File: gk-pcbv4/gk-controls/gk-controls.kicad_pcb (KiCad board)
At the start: 2 copper layers, 120.6 x 72.2 mm, 95 parts, among them J1 Conn_01x20, J2 Conn_01x03, J3 Conn_01x01, J4 Conn_01x01, J5 Conn_01x01, J6 Conn_01x01, U1 PCAL6416APW, U2 ULN2003A

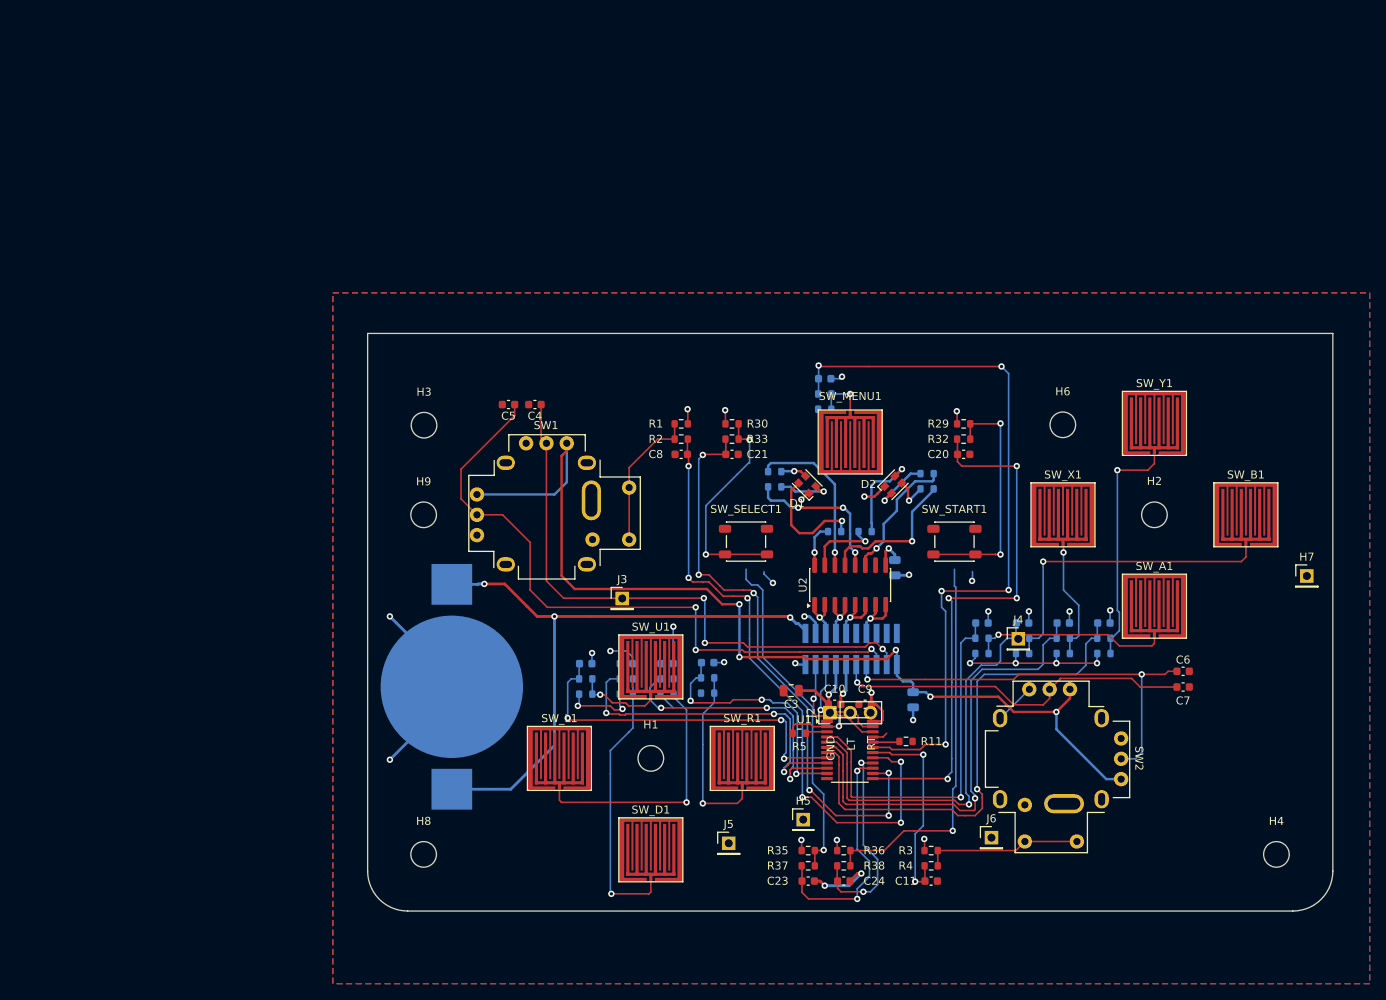
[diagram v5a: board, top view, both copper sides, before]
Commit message: add v3 control board and trigger daughterboard
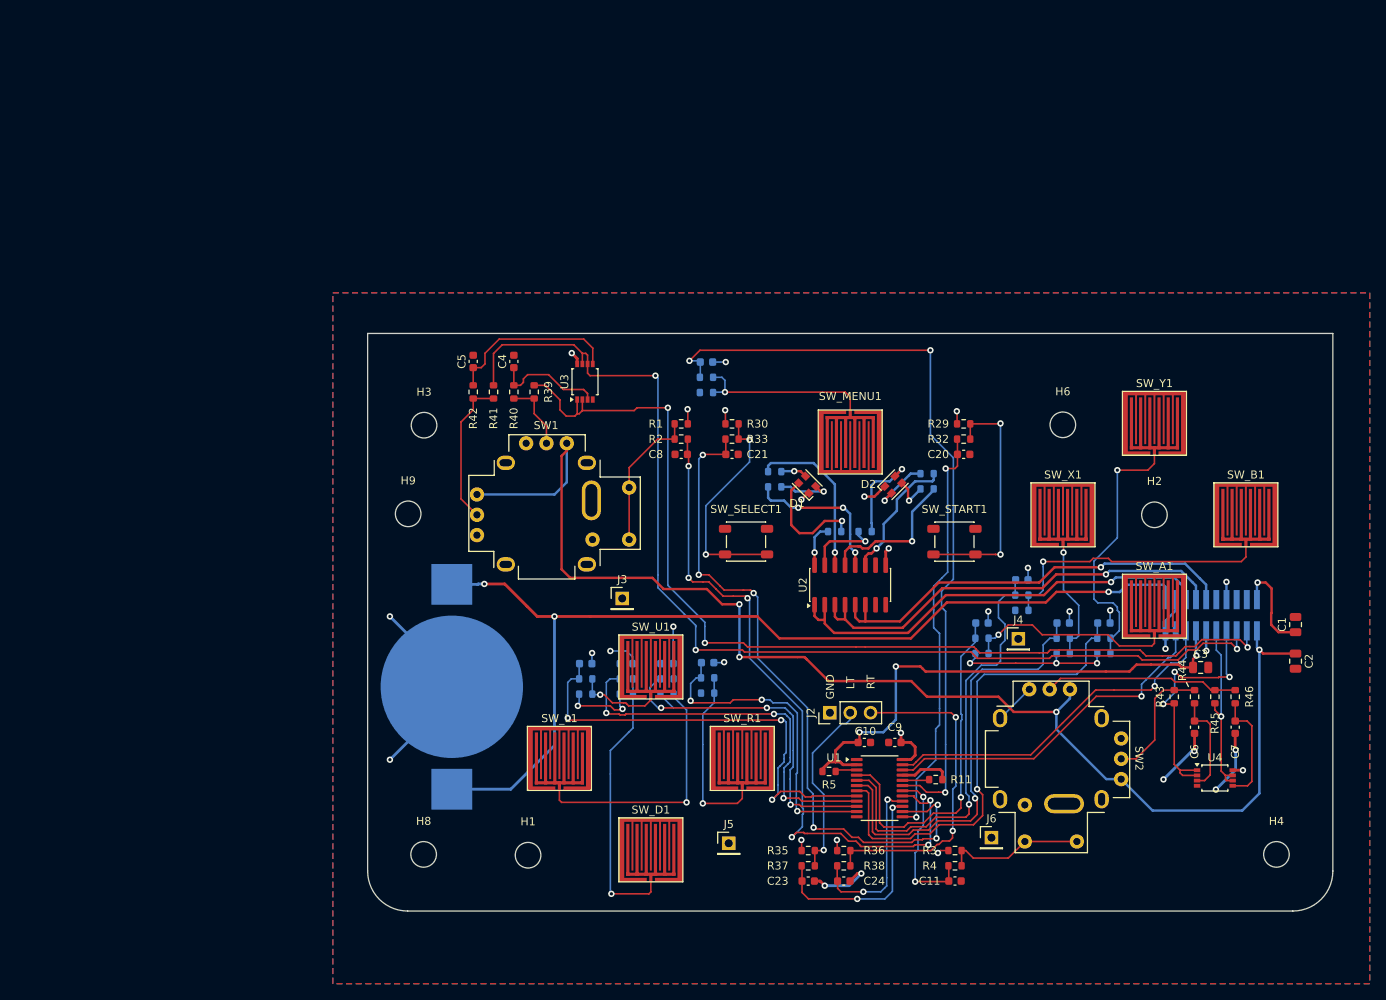
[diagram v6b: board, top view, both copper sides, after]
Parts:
- removed H5, H7: Conn_01x01, Connector_PinHeader_2.54mm:PinHeader_1x01_P2.54mm_Vertical
- added R39: NC, Resistor_SMD:R_0603_1608Metric, F.Cu at (110.5, 67.3)
- added R40: 20k, Resistor_SMD:R_0603_1608Metric, F.Cu at (108.0, 67.3)
- added R41: NC, Resistor_SMD:R_0603_1608Metric, F.Cu at (105.4, 67.3)
- added R42: 20k, Resistor_SMD:R_0603_1608Metric, F.Cu at (102.9, 67.3)
- added R43: NC, Resistor_SMD:R_0603_1608Metric, F.Cu at (190.5, 105.4)
- added R44: 20k, Resistor_SMD:R_0603_1608Metric, F.Cu at (193.0, 105.4)
- added R45: NC, Resistor_SMD:R_0603_1608Metric, F.Cu at (195.6, 105.4)
- added R46: 20k, Resistor_SMD:R_0603_1608Metric, F.Cu at (198.1, 105.4)
- added U3: LMV358DMR2G, Package_SO:OnSemi_Micro8, F.Cu at (116.8, 66.0)
- added U4: LMV358DMR2G, Package_SO:OnSemi_Micro8, F.Cu at (195.6, 115.6)
- C1, C2: moved to F.Cu
- C4, C5, C6, C7: value 10n -> 100n
- moved C3 51.3 mm to (193.8, 101.8), turned to 0 degrees
- moved C1 50.6 mm to (205.7, 96.4), turned to 90 degrees
- moved C2 48.0 mm to (205.7, 101.0)
- moved J1 45.2 mm to (195.1, 95.2)
- moved H1 19.5 mm to (109.7, 125.2)
- moved C22 14.9 mm to (132.0, 63.6)
- moved R31 14.9 mm to (132.0, 67.4)
- moved R34 14.9 mm to (132.0, 65.5)
- moved C7 8.22 mm to (198.1, 109.2), turned to -90 degrees
- moved C6 7.13 mm to (193.0, 109.2), turned to -90 degrees
- moved C5 6.97 mm to (102.9, 63.5), turned to 90 degrees
- moved R11 6.05 mm to (160.7, 115.8)
- moved R5 6.05 mm to (147.4, 114.8)
- moved U1 6.05 mm to (153.7, 116.8)
- moved C10 6.05 mm to (151.8, 111.1)
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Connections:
- C4 pad 1: JOY_A_X -> Net-(U3A-+)
- C5 pad 1: JOY_A_Y -> Net-(U3B-+)
- C6 pad 1: JOY_B_X -> Net-(U4A-+)
- C7 pad 1: JOY_B_Y -> Net-(U4B-+)
- J1 pad 3: JOY_A_X -> JOY_A_X_MCU
- J1 pad 5: JOY_A_Y -> JOY_A_Y_MCU
- J1 pad 7: JOY_B_X -> JOY_B_X_MCU
- J1 pad 9: JOY_B_Y -> JOY_B_Y_MCU
- J3 pad 1: unconnected-(J3-Pin_1-Pad1) -> GND
- J4 pad 1: unconnected-(J4-Pin_1-Pad1) -> GND
- J5 pad 1: unconnected-(J5-Pin_1-Pad1) -> GND
- J6 pad 1: unconnected-(J6-Pin_1-Pad1) -> GND
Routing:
- net JOY_A_Y_MCU: track 0.00 -> 137.2 mm, vias 0 -> 3
- net JOY_A_X_MCU: track 0.00 -> 126.1 mm, vias 0 -> 3
- net JOY_A_X: track 73.7 -> 8.77 mm, vias 3 -> 0
- net JOY_A_Y: track 82.8 -> 18.5 mm, vias 3 -> 0
- net Net-(BT1-+): track 78.3 -> 127.9 mm
- net BTNLED_B: track 6.16 -> 55.7 mm
- net BTNLED_G: track 5.90 -> 54.5 mm
- net BTNLED_R: track 7.25 -> 53.7 mm
- net VDDIO: track 21.1 -> 65.7 mm, vias 2 -> 3
- net VDDA: track 126.1 -> 167.2 mm, vias 5 -> 4
- net JOY_B_X: track 53.7 -> 15.8 mm, vias 2 -> 0
- net JOY_B_X_MCU: track 0.00 -> 32.5 mm, vias 0 -> 3
- net I2C1_SDA: track 13.8 -> 44.8 mm
- net I2C1_SCL: track 14.5 -> 43.8 mm
- net JOY_B_Y_MCU: track 0.00 -> 22.9 mm, vias 0 -> 1
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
